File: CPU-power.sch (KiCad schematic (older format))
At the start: 58 parts, among them U1 MIMX8MM6DVTLZAA

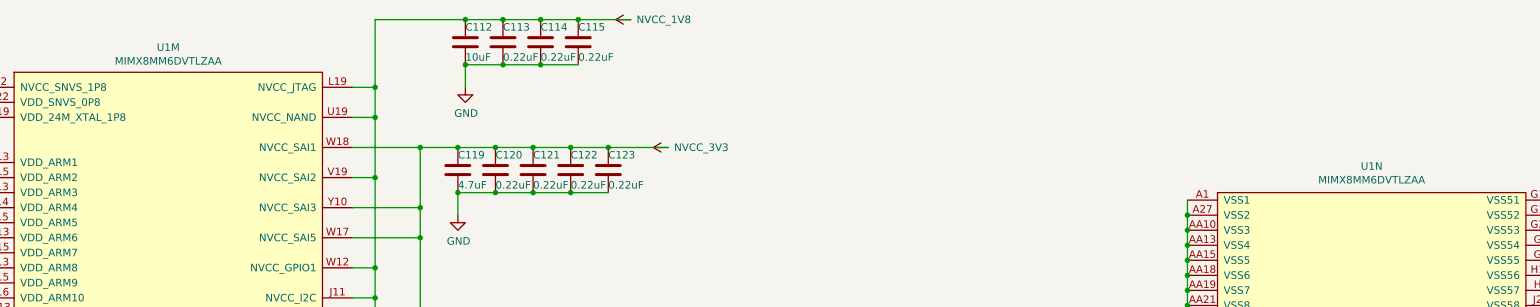
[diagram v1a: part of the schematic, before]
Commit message: Complete entry of bom
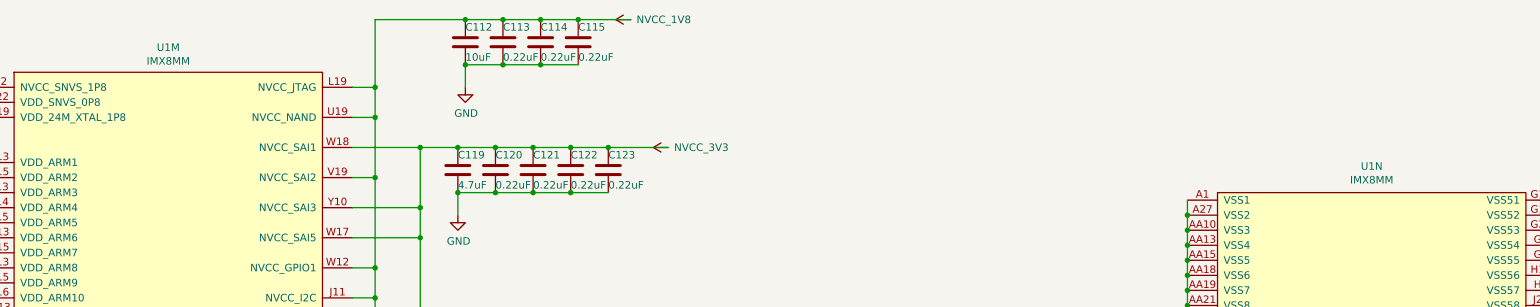
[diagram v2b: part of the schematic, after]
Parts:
- C112, C124, C130, C140, C27, C28, C83, C84: Mfgr (none) -> Murata; Part (none) -> GRM155C80J106ME11D; Vendorpart (none) -> 490-13233-1-ND
- C113, C114, C115, C117, C118, C120, C121, C122, C123, C136, C137, C138, C139, C141, C142, C143, C144, C146, C147, C148: Mfgr (none) -> Murata; Part (none) -> GRM033C80J224KE90D; Vendorpart (none) -> 490-10392-1-ND
- C116, C125, C126, C127, C128, C129, C131, C132, C133, C134, C135, C151, C29, C30, C31, C32, C33, C34, C85, C86, C87, C88, C89, C90: Mfgr (none) -> Murata; Part (none) -> GRM033C80G105ME05D; Vendorpart (none) -> 490-18622-1-ND
- C119, C145: Mfgr (none) -> Murata; Part (none) -> GRM155C80J475MEAAD; Vendorpart (none) -> 490-14458-1-ND
- C149: Mfgr (none) -> Murata; Part (none) -> GRM033D80E225ME47D; Vendorpart (none) -> 490-18653-1-ND
- C150: Mfgr (none) -> Murata; Part (none) -> GRM033R70J222KA01D; Vendorpart (none) -> 490-6142-1-ND
- R38: Mfgr (none) -> Yageo; Part (none) -> RC0402JR-070RL; Vendorpart (none) -> 311-0.0JRCT-ND
- U1: value MIMX8MM6DVTLZAA -> IMX8MM; Mfgr (none) -> NXP; Part (none) -> MIMX8MM6CVTKZAA; Vendorpart (none) -> 568-15276-ND

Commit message: Finish remaining routing
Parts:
- removed R38: 0, Resistor_SMD:R_0402_1005Metric, symbol Device:R
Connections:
- net VDD_MIPI_1P2 is gone; now on net VDD_PHY_1V2: C148.1, C149.1, U1.J15 (VDD_MIPI_1P2)
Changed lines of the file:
@@
 	0    -1   -1   0
 $EndComp
-Wire Wire Line
-	7550 7400 7450 7400
 $Comp
 L mxenc:VDD_PHY_0V9 #PWR0137
@@
 Wire Wire Line
 	7100 7950 7350 7950
-$Comp
-L Device:R R38
-U 1 1 5DDBDDF9
-P 7700 7400
-F 0 "R38" V 7493 7400 50  0000 C CNN
-F 1 "0" V 7584 7400 50  0000 C CNN
-F 2 "Resistor_SMD:R_0402_1005Metric" V 7630 7400 50  0001 C CNN
-F 3 "~" H 7700 7400 50  0001 C CNN
-F 4 "Yageo" H 7700 7400 50  0001 C CNN "Mfgr"
-F 5 "RC0402JR-070RL" H 7700 7400 50  0001 C CNN "Part"
-F 6 "311-0.0JRCT-ND" H 7700 7400 50  0001 C CNN "Vendorpart"
-	1    7700 7400
-	0    1    1    0
-$EndComp
-Wire Wire Line
-	7850 7400 8100 7400
-Text Label 6400 7400 0    50   ~ 0
-VDD_MIPI_1P2
 Wire Wire Line
 	6150 3550 6950 3550
@@
 Wire Wire Line
 	7450 7400 7350 7400
+Wire Wire Line
+	7450 7400 8100 7400
 $EndSCHEMATC

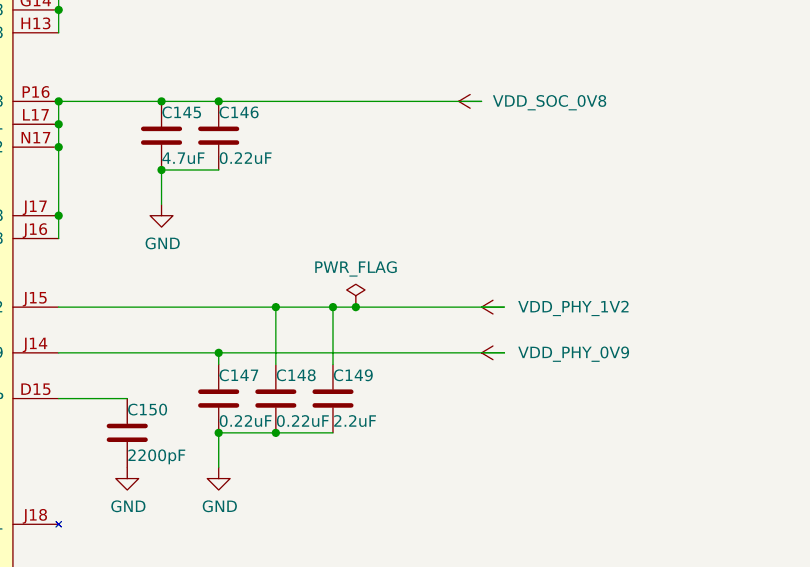
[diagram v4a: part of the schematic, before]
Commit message: Set up for battery NTC and add a power button
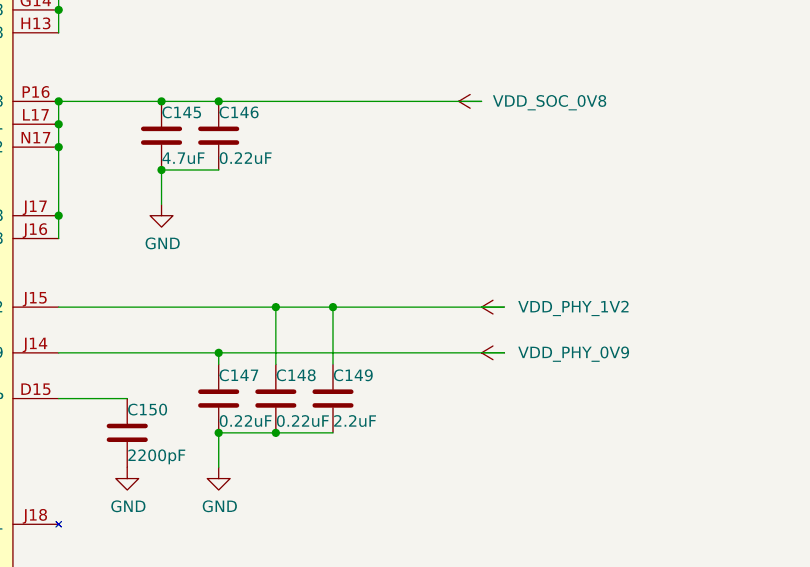
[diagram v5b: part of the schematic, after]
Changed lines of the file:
@@
 EESchema Schematic File Version 4
-LIBS:mxenc-cache
-EELAYER 29 0
+EELAYER 30 0
 EELAYER END
 $Descr USLedger 17000 11000
 encoding utf-8
 Sheet 3 10
-Title ""
-Date ""
-Rev ""
-Comp ""
+Title "kimχ micro"
+Date "2020-03-05"
+Rev "0.9"
+Comp "GroupGets"
 Comment1 ""
 Comment2 ""
@@
 	0    -1   -1   0
 $EndComp
-$Comp
-L power:PWR_FLAG #FLG0111
-U 1 1 5E0DCDB6
-P 7450 7400
-F 0 "#FLG0111" H 7450 7475 50  0001 C CNN
-F 1 "PWR_FLAG" H 7450 7573 50  0000 C CNN
-F 2 "" H 7450 7400 50  0001 C CNN
-F 3 "~" H 7450 7400 50  0001 C CNN
-	1    7450 7400
-	1    0    0    -1
-$EndComp
-Connection ~ 7450 7400
-Wire Wire Line
-	7450 7400 7350 7400
-Wire Wire Line
-	7450 7400 8100 7400
+Wire Wire Line
+	7350 7400 8100 7400
 $EndSCHEMATC

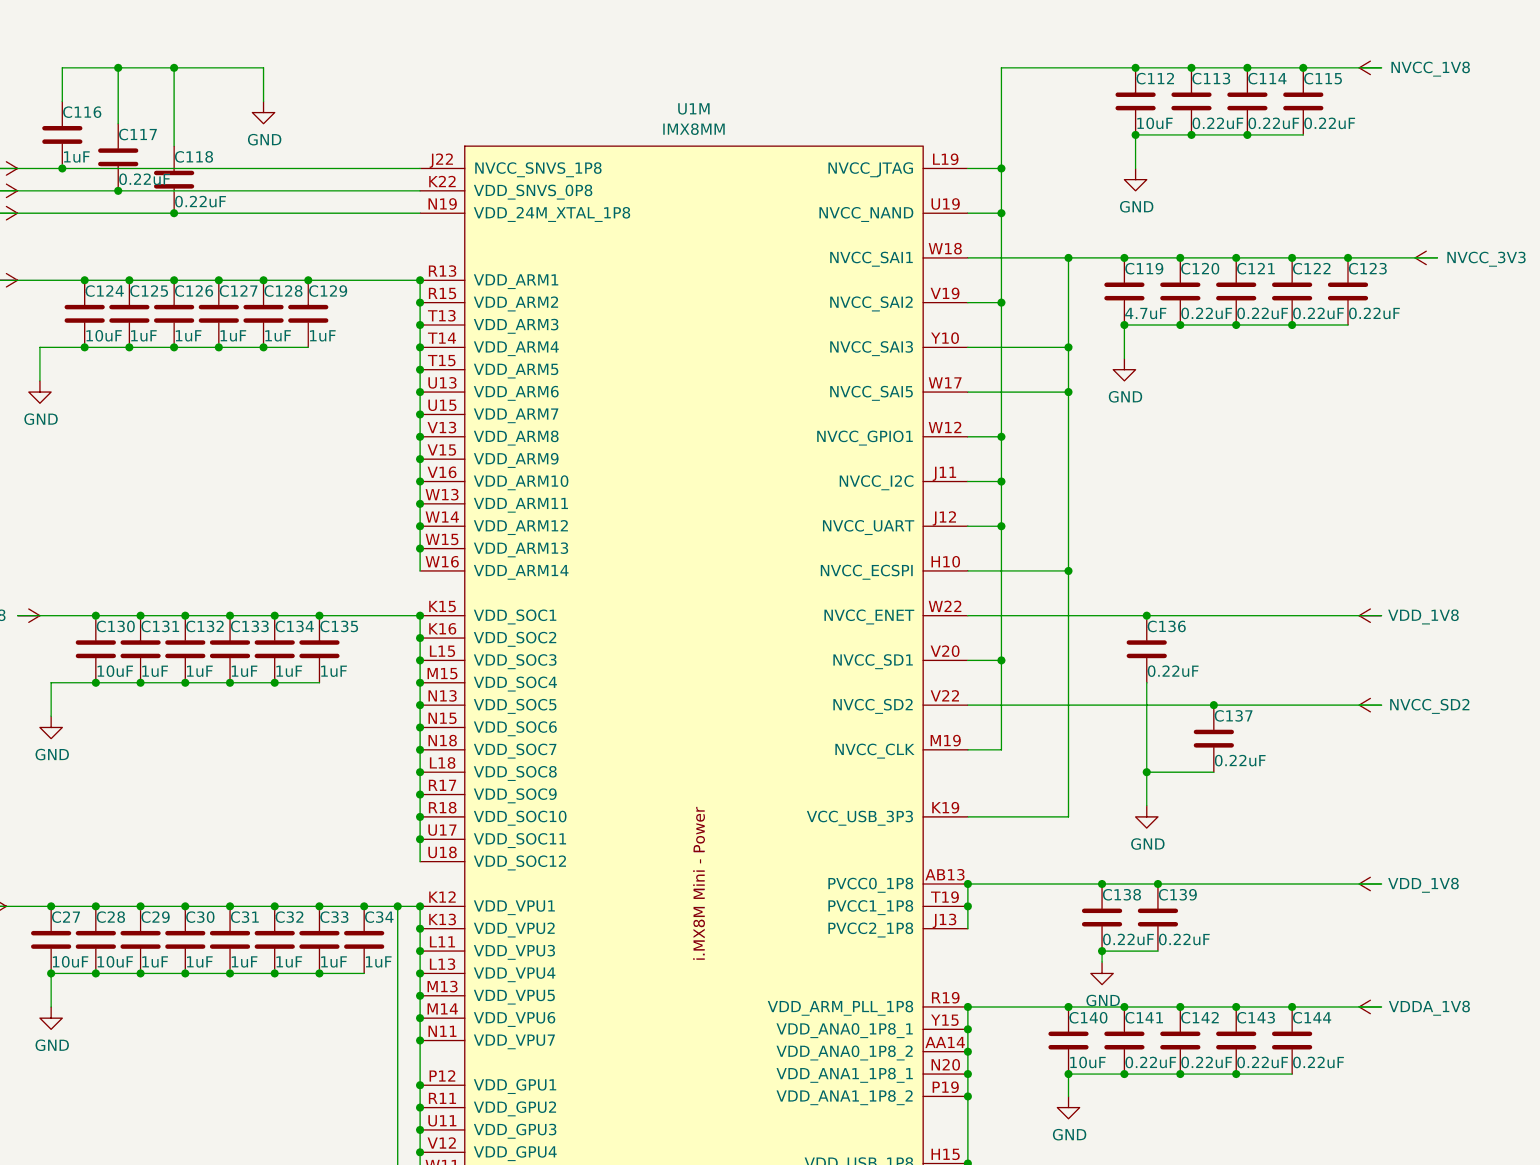
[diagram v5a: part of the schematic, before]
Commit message: Cleanup remaining DRC problems from schematic
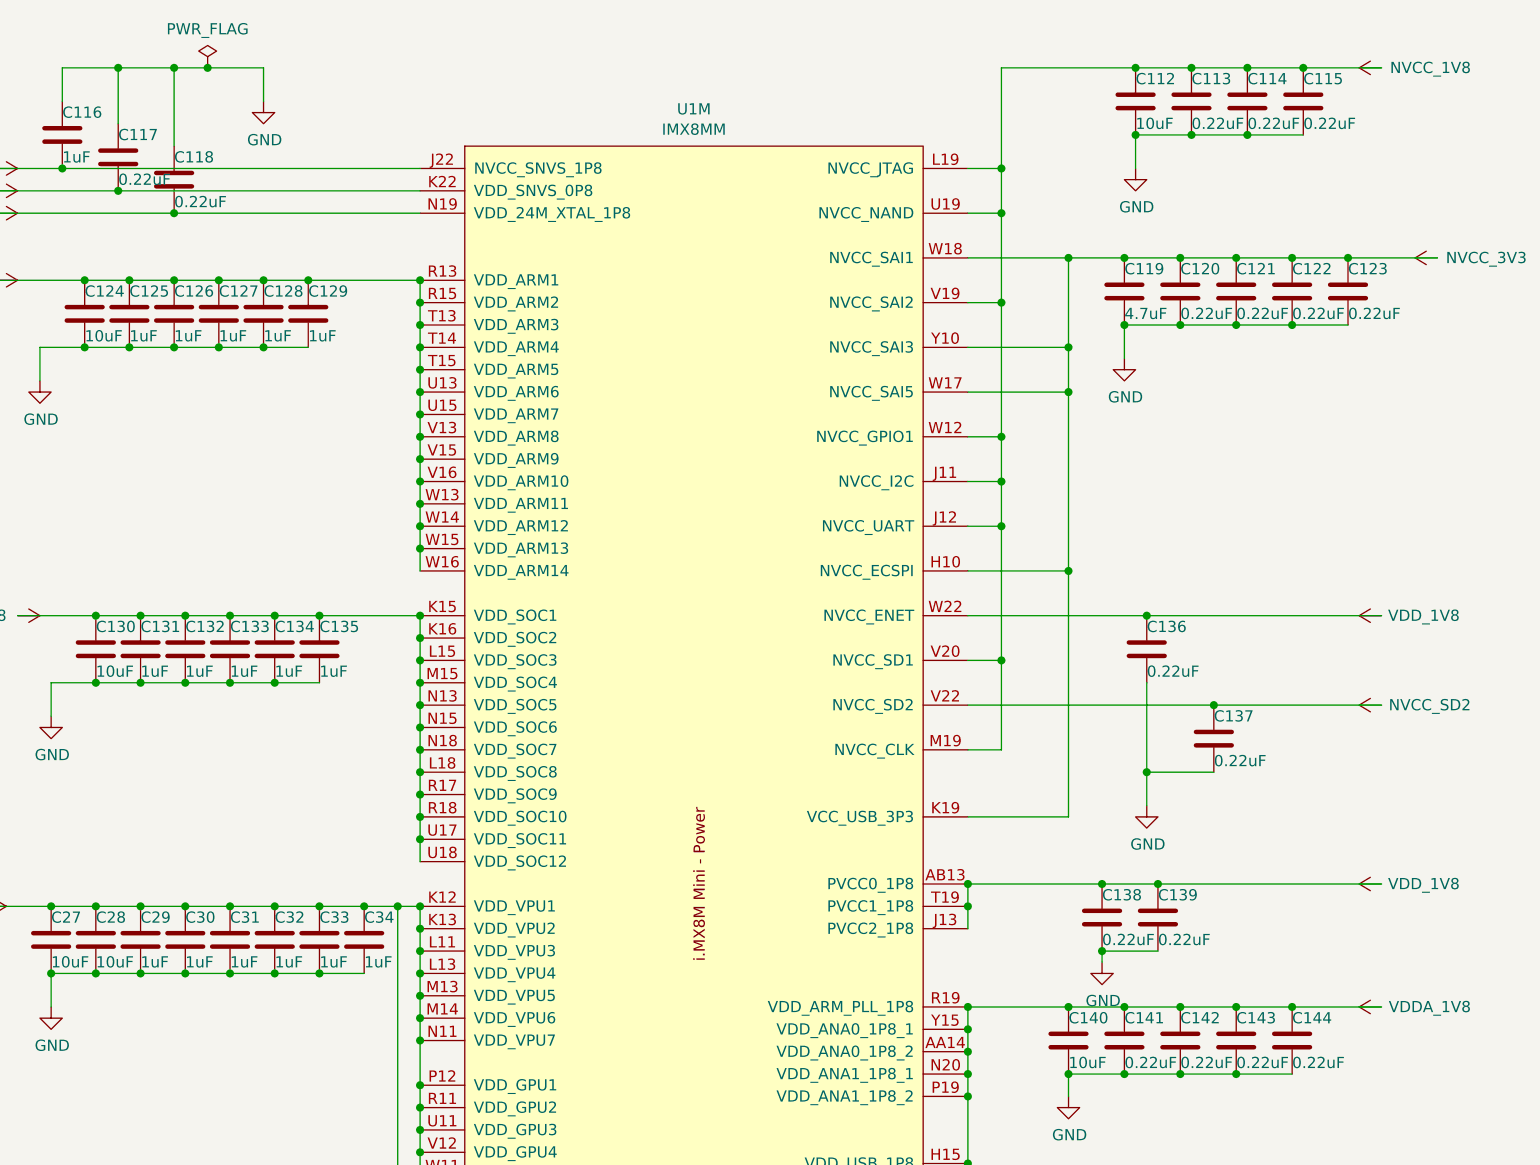
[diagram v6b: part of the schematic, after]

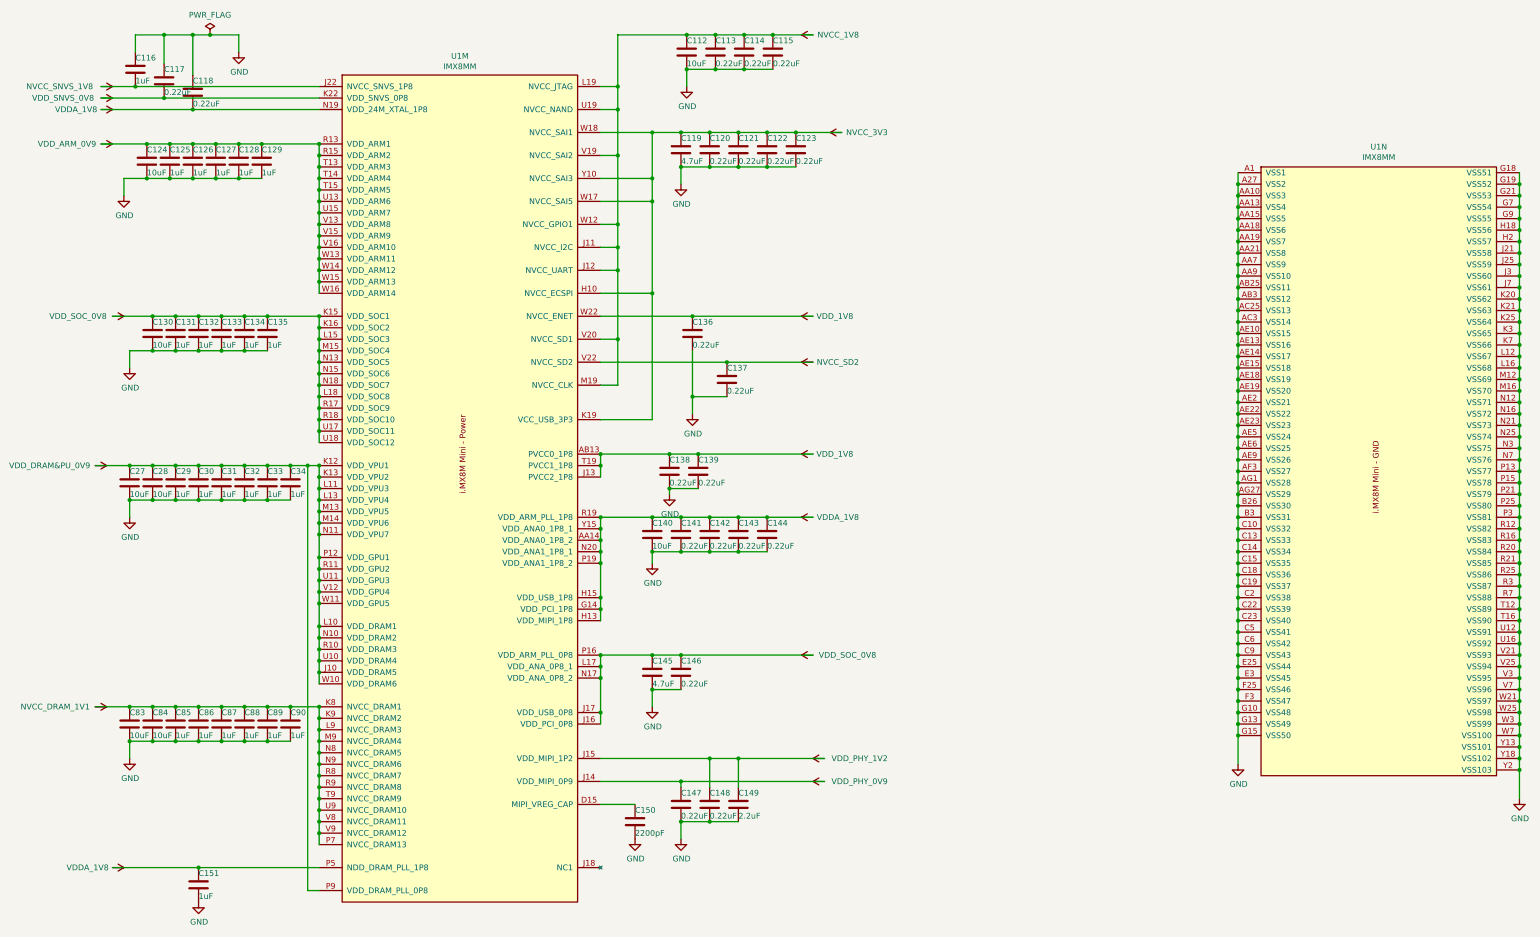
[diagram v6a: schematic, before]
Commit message: Re-annotate schematics, add dnp field, and silkscreen cleanup
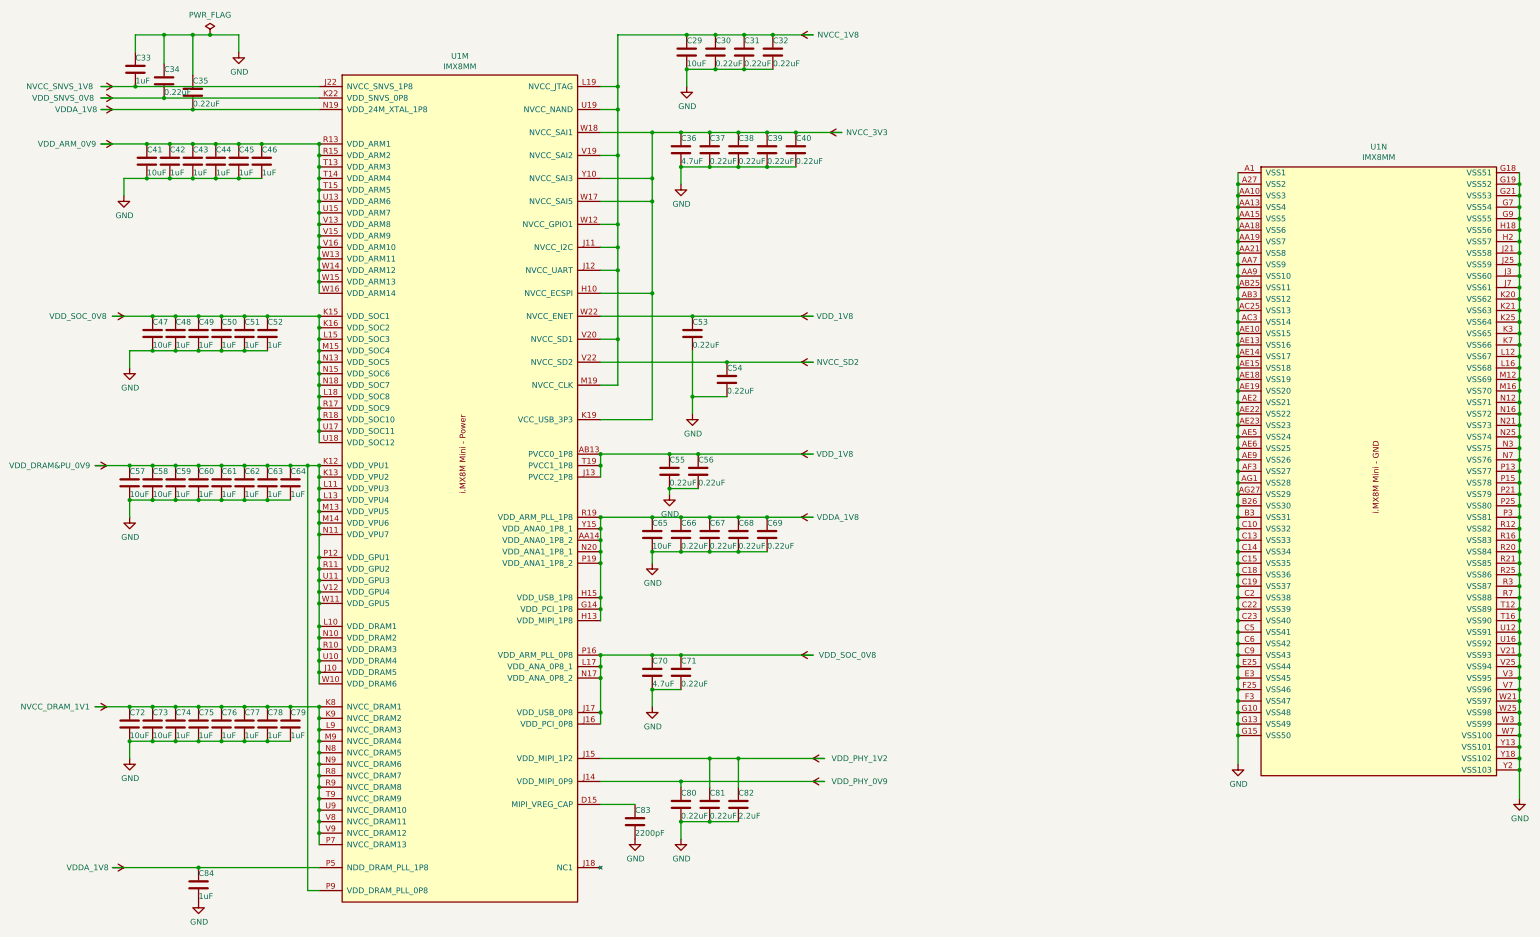
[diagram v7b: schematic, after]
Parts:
- renumbered C112 to C29, C113 to C30, C114 to C31, C115 to C32, C116 to C33, C117 to C34, C118 to C35, C119 to C36, C120 to C37, C121 to C38, C122 to C39, C123 to C40, C124 to C41, C125 to C42, C126 to C43, C127 to C44, C128 to C45, C129 to C46, C130 to C47, C131 to C48, C132 to C49, C133 to C50, C134 to C51, C135 to C52, C136 to C53, C137 to C54, C138 to C55, C139 to C56, C27 to C57, C28 to C58, C29 to C59, C30 to C60, C31 to C61, C32 to C62, C33 to C63, C34 to C64, C140 to C65, C141 to C66, C142 to C67, C143 to C68, C144 to C69, C145 to C70, C146 to C71, C83 to C72, C84 to C73, C85 to C74, C86 to C75, C87 to C76, C88 to C77, C89 to C78, C90 to C79, C147 to C80, C148 to C81, C149 to C82, C150 to C83, C151 to C84
